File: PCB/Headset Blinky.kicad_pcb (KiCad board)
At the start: 2 copper layers, 98.9 x 74.9 mm, 19 parts, among them J1 Conn_01x02_Socket, J2 Conn_01x01_Socket, U1 NE555P, U2 4017

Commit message: Updated PCB files!
Updated the routing - This will be the final routing of the PCB
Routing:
- net Net-(D1-K): track 10.7 -> 115.4 mm
- net Net-(D9-A): track 0.00 -> 46.1 mm, vias 0 -> 2
- net Net-(D8-A): track 0.00 -> 43.4 mm
- net Net-(D10-A): track 0.57 -> 43.2 mm
- net Net-(D7-A): track 0.00 -> 38.2 mm
- net +5V: track 32.5 -> 0.00 mm
- net Net-(U1-DISCH): track 0.00 -> 29.2 mm
- net Net-(D1-A): track 0.00 -> 29.1 mm
- net Net-(D5-A): track 0.00 -> 26.2 mm, vias 0 -> 1
- net GND: track 17.6 -> 41.2 mm
- net Net-(D2-A): track 0.00 -> 22.8 mm, vias 0 -> 2
- net TR: track 5.30 -> 27.5 mm
- net Net-(D4-A): track 0.00 -> 22.0 mm
- net Net-(D6-A): track 0.00 -> 21.9 mm
- net Net-(D3-A): track 0.00 -> 15.0 mm, vias 0 -> 2
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- added copper zone on F.Cu, net +5V
- added copper zone on B.Cu, net GND

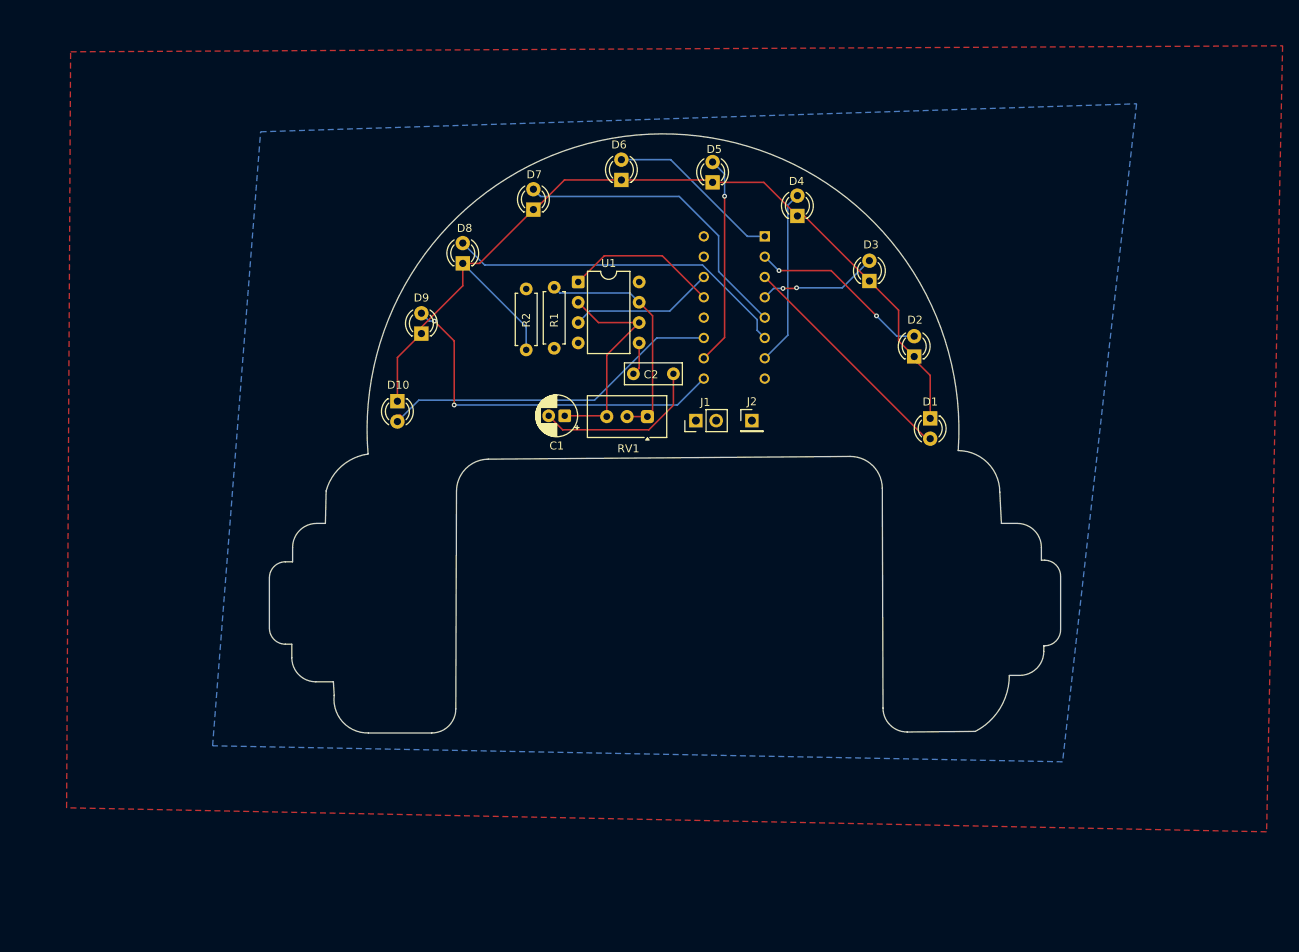
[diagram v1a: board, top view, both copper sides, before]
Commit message: Updated PCB Files
Updated routing and added art!
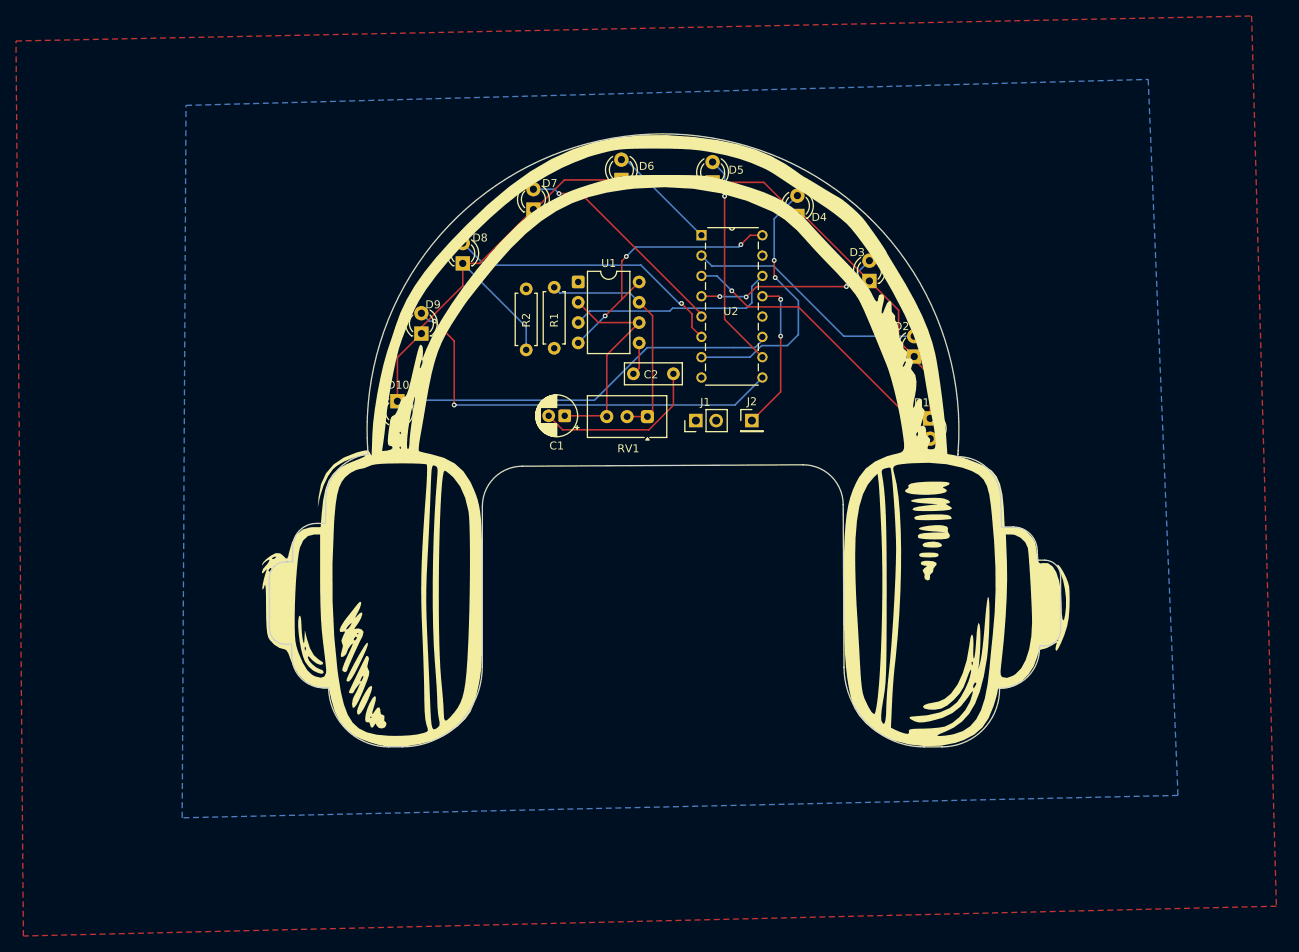
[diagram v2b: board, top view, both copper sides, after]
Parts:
- added G***: LOGO, LOGO, F.Cu at (145.2, 79.6)
- added G***: LOGO, LOGO, B.Cu at (111.3, 97.7)
- added a: LOGO, LOGO, B.Cu at (180.8, 99.3)
- U2: moved to F.Cu
- moved U2 7.33 mm to (158.2, 70.0), turned to 0 degrees
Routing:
- net +5V: track 0.00 -> 34.5 mm, vias 0 -> 3
- net Net-(D4-A): track 22.0 -> 33.1 mm, vias 0 -> 2
- net Net-(D7-A): track 38.2 -> 27.8 mm, vias 0 -> 1
- net OUT: track 18.1 -> 26.6 mm
- net Net-(D3-A): track 15.0 -> 23.1 mm, vias 2 -> 3
- net Net-(D1-A): track 29.1 -> 37.0 mm, vias 0 -> 1
- net Net-(D6-A): track 21.9 -> 13.9 mm
- net Net-(D2-A): track 22.8 -> 30.8 mm, vias 2 -> 0
- net Net-(D10-A): track 43.2 -> 50.8 mm
- net Net-(D9-A): track 46.1 -> 53.5 mm
- net Net-(D8-A): track 43.4 -> 36.3 mm, vias 0 -> 1
- net Net-(D5-A): track 26.2 -> 27.0 mm
- net GND: track 41.2 -> 40.7 mm, vias 0 -> 2
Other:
- board size 98.9 x 74.9 mm -> 98.9 x 76.6 mm
- board text added: "@Mirai_09 :)"
- board text added: "Headset Blinky!"
- board text added: "Music <3"
